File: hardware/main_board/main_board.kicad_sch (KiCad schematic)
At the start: 0 parts

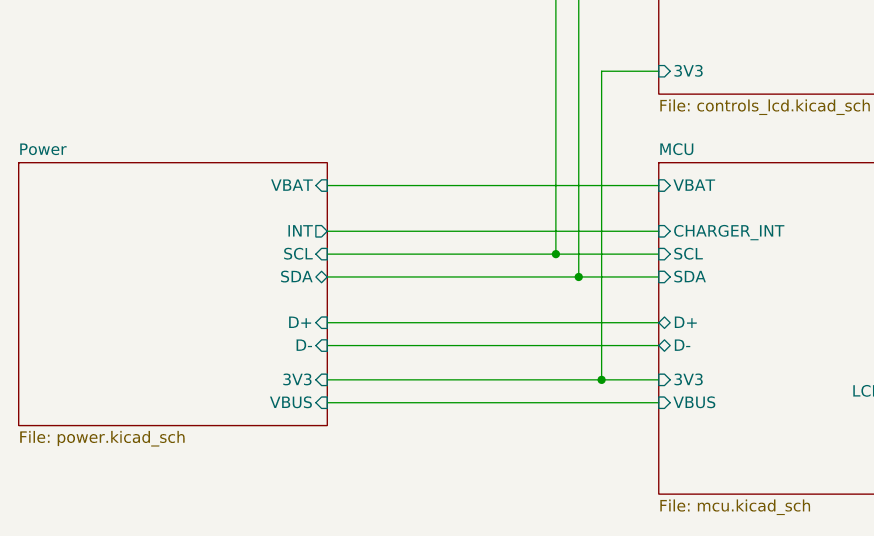
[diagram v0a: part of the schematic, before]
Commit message: Add SYS power to the extension socket
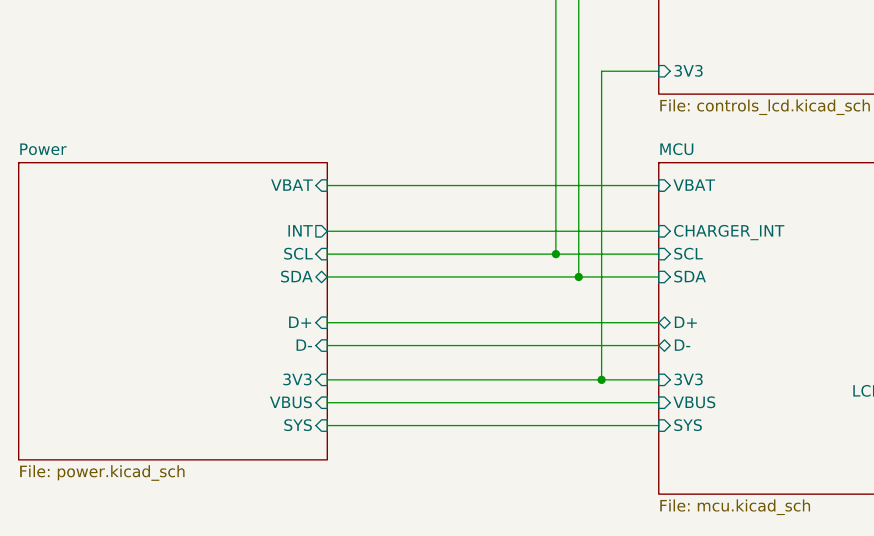
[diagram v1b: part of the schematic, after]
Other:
- sheet MCU ports: added SYS; removed none
- sheet Power ports: added SYS; removed none
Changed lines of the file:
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@@
+	(wire
+		(pts
+			(xy 63.5 123.19) (xy 100.33 123.19)
+		)
+		(stroke
+			(width 0)
+			(type default)
+		)
+	)
 	(wire
 		(pts
@@
 			)
 		)
+		(pin "SYS" input
+			(at 100.33 123.19 180)
+			(effects
+				(font
+					(size 1.27 1.27)
+				)
+				(justify left)
+			)
+		)
 		(instances
 			(project "main_board"
@@
 	(sheet
 		(at 29.21 93.98)
-		(size 34.29 29.21)
+		(size 34.29 33.02)
 		(exclude_from_sim no)
 		(in_bom yes)
@@
 		)
 		(property "Sheetfile" "power.kicad_sch"
-			(at 29.21 123.7746 0)
+			(at 29.21 127.5846 0)
 			(effects
 				(font
@@
 			(effects
 				(font
+					(size 1.27 1.27)
+				)
+				(justify right)
+			)
+		)
+		(pin "SYS" input
+			(at 63.5 123.19 0)
+			(effects
+				(font
